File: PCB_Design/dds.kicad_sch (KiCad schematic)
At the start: 56 parts, among them U6 AD9106BCP, U7 ADA4817-2ACPZ-R7, U8 ADA4817-2ACPZ-R7

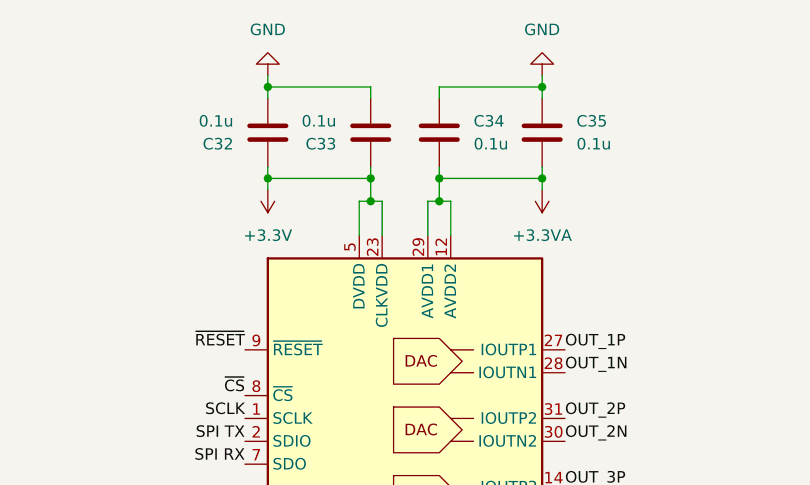
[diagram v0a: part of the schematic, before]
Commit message: KiCAD file update, completed PCB
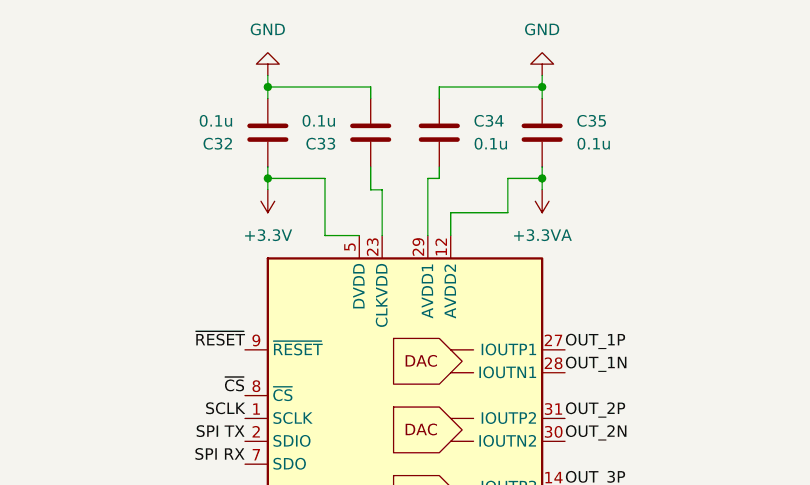
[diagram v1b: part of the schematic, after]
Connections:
- net +3.3V: no longer C33.1, U6.23 (CLKVDD)
- net +3.3VA: no longer C34.2, U6.29 (AVDD1)
- new net: C33.1, U6.23 (CLKVDD)
- new net: C34.2, U6.29 (AVDD1)
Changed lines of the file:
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@@
   (junction (at 180.34 72.39) (diameter 0) (color 0 0 0 0)
   )
-  (junction (at 100.33 33.02) (diameter 0) (color 0 0 0 0)
-  )
   (junction (at 81.28 30.48) (diameter 0) (color 0 0 0 0)
   )
@@
   (junction (at 180.34 129.54) (diameter 0) (color 0 0 0 0)
   )
-  (junction (at 92.71 33.02) (diameter 0) (color 0 0 0 0)
-  )
   (junction (at 250.19 48.26) (diameter 0) (color 0 0 0 0)
   )
@@
   (junction (at 118.11 82.55) (diameter 0) (color 0 0 0 0)
   )
-  (junction (at 92.71 30.48) (diameter 0) (color 0 0 0 0)
-  )
   (junction (at 168.91 144.78) (diameter 0) (color 0 0 0 0)
   )
@@
   )
   (junction (at 180.34 67.31) (diameter 0) (color 0 0 0 0)
-  )
-  (junction (at 100.33 30.48) (diameter 0) (color 0 0 0 0)
   )
   (junction (at 250.19 43.18) (diameter 0) (color 0 0 0 0)
@@
     (stroke (width 0) (type default))
   )
-  (wire (pts (xy 92.71 29.21) (xy 92.71 30.48))
-    (stroke (width 0) (type default))
-  )
   (wire (pts (xy 250.19 110.49) (xy 257.81 110.49))
     (stroke (width 0) (type default))
@@
     (stroke (width 0) (type default))
   )
-  (wire (pts (xy 92.71 33.02) (xy 91.44 33.02))
-    (stroke (width 0) (type default))
-  )
   (wire (pts (xy 241.3 106.68) (xy 245.11 106.68))
     (stroke (width 0) (type default))
@@
     (stroke (width 0) (type default))
   )
-  (wire (pts (xy 100.33 33.02) (xy 99.06 33.02))
+  (wire (pts (xy 100.33 30.48) (xy 99.06 30.48))
     (stroke (width 0) (type default))
   )
@@
     (stroke (width 0) (type default))
   )
-  (wire (pts (xy 101.6 33.02) (xy 101.6 36.83))
+  (wire (pts (xy 101.6 34.29) (xy 101.6 36.83))
     (stroke (width 0) (type default))
   )
@@
     (stroke (width 0) (type default))
   )
+  (wire (pts (xy 107.95 30.48) (xy 111.76 30.48))
+    (stroke (width 0) (type default))
+  )
   (wire (pts (xy 180.34 67.31) (xy 196.85 67.31))
     (stroke (width 0) (type default))
   )
-  (wire (pts (xy 93.98 33.02) (xy 93.98 36.83))
+  (wire (pts (xy 93.98 31.75) (xy 93.98 36.83))
     (stroke (width 0) (type default))
   )
@@
     (stroke (width 0) (type default))
   )
-  (wire (pts (xy 81.28 30.48) (xy 92.71 30.48))
+  (wire (pts (xy 81.28 30.48) (xy 87.63 30.48))
     (stroke (width 0) (type default))
   )
@@
     (stroke (width 0) (type default))
   )
+  (wire (pts (xy 87.63 36.83) (xy 91.44 36.83))
+    (stroke (width 0) (type default))
+  )
   (wire (pts (xy 180.34 66.04) (xy 180.34 67.31))
     (stroke (width 0) (type default))
@@
     (stroke (width 0) (type default))
   )
-  (wire (pts (xy 100.33 30.48) (xy 111.76 30.48))
-    (stroke (width 0) (type default))
-  )
   (wire (pts (xy 72.39 90.17) (xy 78.74 90.17))
     (stroke (width 0) (type default))
@@
     (stroke (width 0) (type default))
   )
-  (wire (pts (xy 100.33 33.02) (xy 101.6 33.02))
-    (stroke (width 0) (type default))
-  )
-  (wire (pts (xy 92.71 30.48) (xy 92.71 33.02))
+  (wire (pts (xy 107.95 34.29) (xy 101.6 34.29))
     (stroke (width 0) (type default))
   )
@@
     (stroke (width 0) (type default))
   )
+  (wire (pts (xy 107.95 30.48) (xy 107.95 34.29))
+    (stroke (width 0) (type default))
+  )
   (wire (pts (xy 111.76 177.8) (xy 115.57 177.8))
     (stroke (width 0) (type default))
@@
     (stroke (width 0) (type default))
   )
-  (wire (pts (xy 91.44 33.02) (xy 91.44 36.83))
+  (wire (pts (xy 87.63 30.48) (xy 87.63 36.83))
     (stroke (width 0) (type default))
   )
@@
     (stroke (width 0) (type default))
   )
-  (wire (pts (xy 100.33 30.48) (xy 100.33 33.02))
-    (stroke (width 0) (type default))
-  )
   (wire (pts (xy 250.19 57.15) (xy 250.19 58.42))
     (stroke (width 0) (type default))
@@
     (stroke (width 0) (type default))
   )
+  (wire (pts (xy 93.98 31.75) (xy 92.71 31.75))
+    (stroke (width 0) (type default))
+  )
   (wire (pts (xy 93.98 99.06) (xy 93.98 97.79))
     (stroke (width 0) (type default))
@@
     (stroke (width 0) (type default))
   )
+  (wire (pts (xy 92.71 31.75) (xy 92.71 29.21))
+    (stroke (width 0) (type default))
+  )
   (wire (pts (xy 245.11 110.49) (xy 250.19 110.49))
     (stroke (width 0) (type default))
@@
     (stroke (width 0) (type default))
   )
-  (wire (pts (xy 92.71 33.02) (xy 93.98 33.02))
-    (stroke (width 0) (type default))
-  )
   (wire (pts (xy 245.11 109.22) (xy 241.3 109.22))
     (stroke (width 0) (type default))
@@
     (stroke (width 0) (type default))
   )
-  (wire (pts (xy 99.06 33.02) (xy 99.06 36.83))
-    (stroke (width 0) (type default))
-  )
+  (wire (pts (xy 99.06 30.48) (xy 99.06 36.83))
+    (stroke (width 0) (type default))
+  )

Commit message: Slight board updates - Added board PDFs and images
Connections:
- net +3.3V: now also C33.1, U6.23 (CLKVDD)
- net +3.3VA: now also C34.2, U6.29 (AVDD1)
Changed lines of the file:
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@@
   (junction (at 125.73 118.11) (diameter 0) (color 0 0 0 0)
   )
+  (junction (at 101.6 34.29) (diameter 0) (color 0 0 0 0)
+  )
   (junction (at 180.34 134.62) (diameter 0) (color 0 0 0 0)
   )
@@
   (junction (at 168.91 57.15) (diameter 0) (color 0 0 0 0)
   )
+  (junction (at 92.71 30.48) (diameter 0) (color 0 0 0 0)
+  )
   (junction (at 180.34 129.54) (diameter 0) (color 0 0 0 0)
   )
@@
   (junction (at 125.73 158.75) (diameter 0) (color 0 0 0 0)
   )
+  (junction (at 91.44 30.48) (diameter 0) (color 0 0 0 0)
+  )
   (junction (at 125.73 168.91) (diameter 0) (color 0 0 0 0)
   )
   (junction (at 250.19 105.41) (diameter 0) (color 0 0 0 0)
+  )
+  (junction (at 99.06 34.29) (diameter 0) (color 0 0 0 0)
   )
   (no_connect (at 241.3 62.23))
@@
     (stroke (width 0) (type default))
   )
+  (wire (pts (xy 99.06 34.29) (xy 101.6 34.29))
+    (stroke (width 0) (type default))
+  )
   (wire (pts (xy 25.4 15.24) (xy 27.94 15.24))
     (stroke (width 0) (type default))
@@
     (stroke (width 0) (type default))
   )
-  (wire (pts (xy 93.98 31.75) (xy 93.98 36.83))
+  (wire (pts (xy 93.98 30.48) (xy 93.98 36.83))
     (stroke (width 0) (type default))
   )
@@
     (stroke (width 0) (type default))
   )
-  (wire (pts (xy 81.28 30.48) (xy 87.63 30.48))
+  (wire (pts (xy 81.28 30.48) (xy 91.44 30.48))
     (stroke (width 0) (type default))
   )
@@
     (stroke (width 0) (type default))
   )
-  (wire (pts (xy 87.63 36.83) (xy 91.44 36.83))
-    (stroke (width 0) (type default))
-  )
   (wire (pts (xy 180.34 66.04) (xy 180.34 67.31))
     (stroke (width 0) (type default))
@@
     (stroke (width 0) (type default))
   )
-  (wire (pts (xy 87.63 30.48) (xy 87.63 36.83))
+  (wire (pts (xy 91.44 30.48) (xy 91.44 36.83))
     (stroke (width 0) (type default))
   )
@@
     (stroke (width 0) (type default))
   )
-  (wire (pts (xy 93.98 31.75) (xy 92.71 31.75))
+  (wire (pts (xy 93.98 30.48) (xy 92.71 30.48))
     (stroke (width 0) (type default))
   )
@@
     (stroke (width 0) (type default))
   )
+  (wire (pts (xy 99.06 34.29) (xy 99.06 36.83))
+    (stroke (width 0) (type default))
+  )
   (wire (pts (xy 168.91 57.15) (xy 168.91 58.42))
     (stroke (width 0) (type default))
@@
     (stroke (width 0) (type default))
   )
-  (wire (pts (xy 92.71 31.75) (xy 92.71 29.21))
+  (wire (pts (xy 92.71 30.48) (xy 92.71 29.21))
     (stroke (width 0) (type default))
   )
@@
     (stroke (width 0) (type default))
   )
-  (wire (pts (xy 99.06 30.48) (xy 99.06 36.83))
+  (wire (pts (xy 99.06 30.48) (xy 99.06 34.29))
     (stroke (width 0) (type default))
   )
@@
     (stroke (width 0) (type default))
   )
+  (wire (pts (xy 91.44 30.48) (xy 92.71 30.48))
+    (stroke (width 0) (type default))
+  )
